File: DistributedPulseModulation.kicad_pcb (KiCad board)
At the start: 2 copper layers, 95.9 x 90.2 mm, 63 parts, among them IC1 SN7447a, J1 Conn_02x12_Odd_Even, J2 Conn_01x01, U1 74LS251, U10 4053, U11 4053, U12 4053, U2 4013, U25 74LS85, U28 74LS85, U31 74LS85, U4 MCP23017_SP, U7 4053, U8 4040, U9 4040

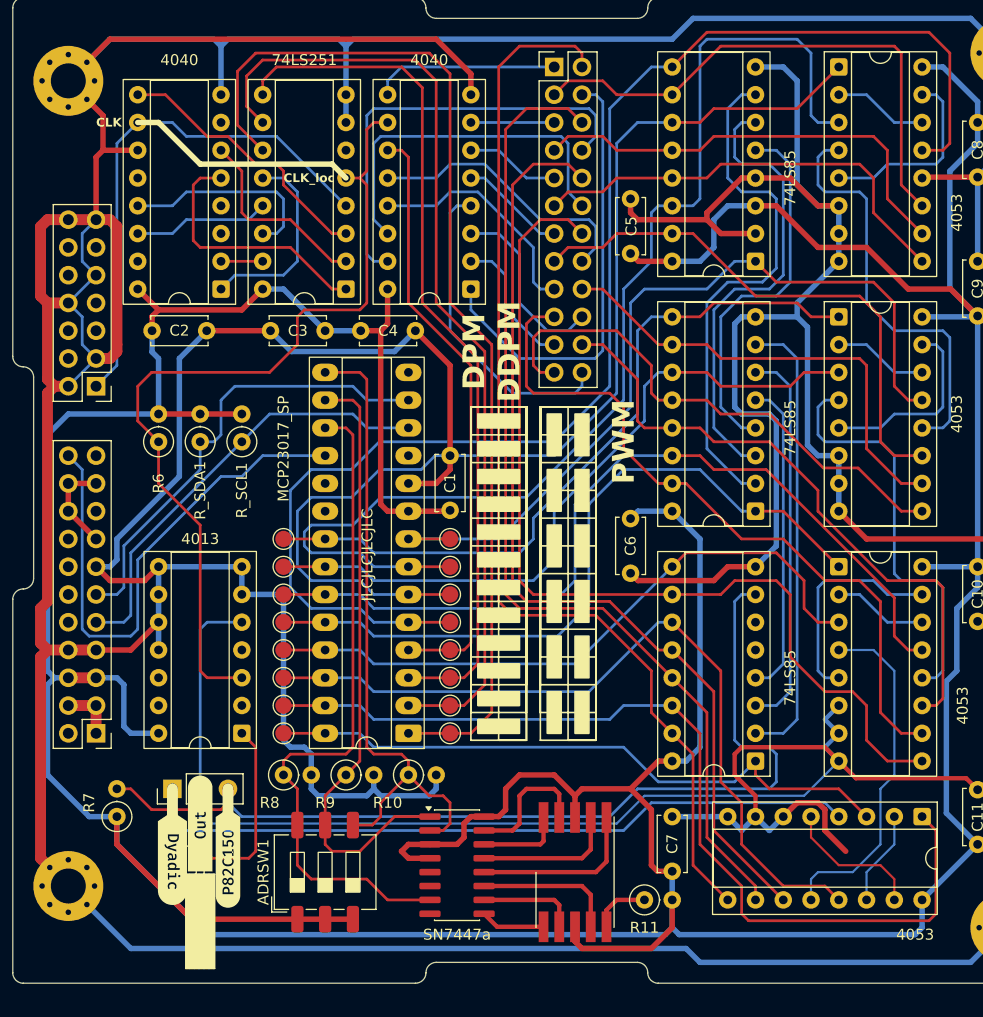
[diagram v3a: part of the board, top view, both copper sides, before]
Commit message: [update] : choix aficheurs et conv ; bug pin A1 ; condo ; doc pdf
- choix du 7-segment en common anode
- choix de decodeur DCBN vers 7-segments
- bug routage pin A1 sur V2.0 de la carte
- condo découplage sur D-latch
- condo découplage sur DVBN->7-segments
- ajout doc pdf work-in-progress
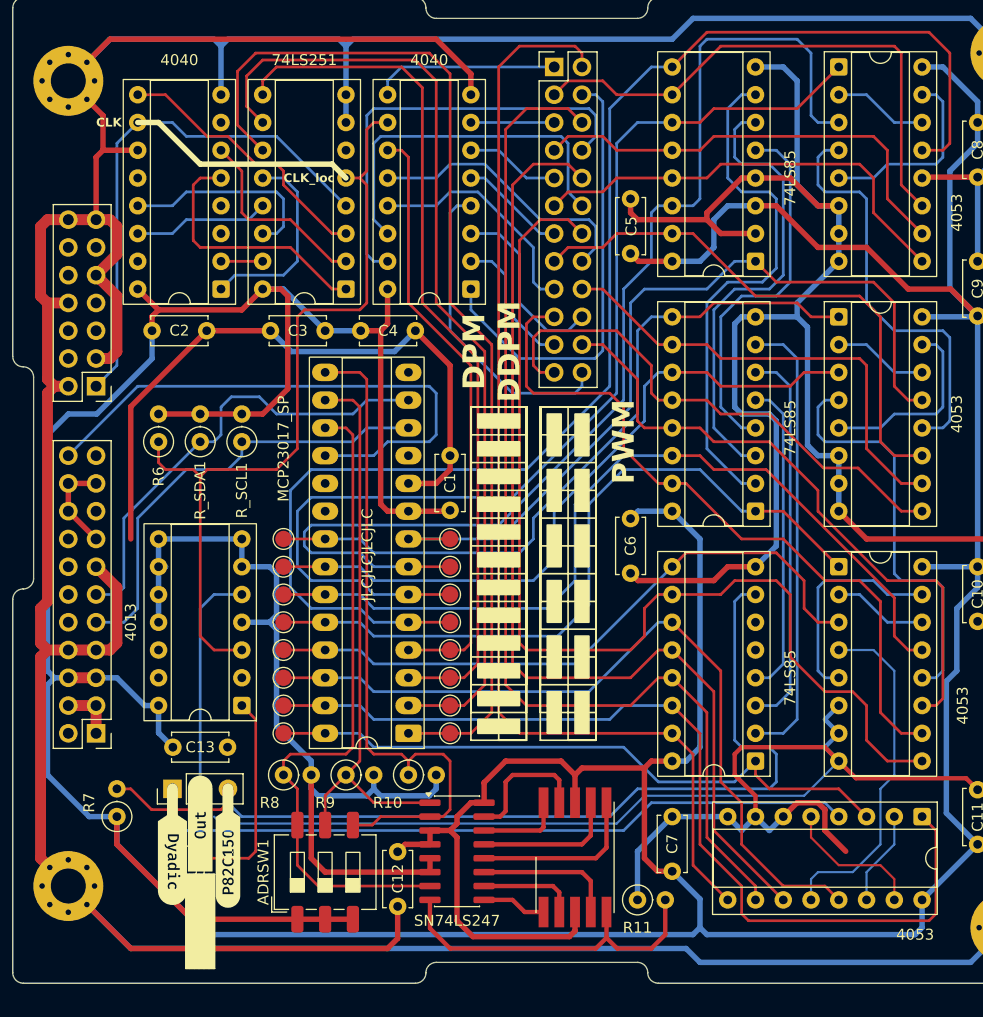
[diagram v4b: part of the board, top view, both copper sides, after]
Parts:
- added C12: 0.1µF, Capacitor_THT:C_Disc_D5.0mm_W2.5mm_P5.00mm, F.Cu at (76.5, 127.6)
- added C13: 0.1µF, Capacitor_THT:C_Disc_D5.0mm_W2.5mm_P5.00mm, F.Cu at (60.9, 113.0)
- DS1: value GS2011CR-G -> GS2011AR-G
- IC1: value SN7447a -> SN74LS247
- R11: value 2.2K -> 330
- moved U2 2.53 mm to (62.2, 109.2)
- moved DS1 1.35 mm to (92.7, 123.1)
- moved IC1 1.27 mm to (81.9, 122.6)
- moved R11 0.64 mm to (98.4, 127.0)
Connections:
- IC1 pad 8: Ground -> Net-(DS1-DP)
- R11 pad 1: Net-(DS1-DP) -> Ground
- R11 pad 2: +5V -> Net-(DS1-DP)
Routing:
- net Ground: track 866.4 -> 909.2 mm
- net Net-(DS1-DP): track 5.39 -> 31.8 mm
- net +5V: track 475.3 -> 497.1 mm
- net /CNT_A3: track 88.1 -> 97.1 mm
- net /CNT_A1: track 92.7 -> 99.7 mm
- net /CNT_A2: track 88.5 -> 94.7 mm
- net /ADR1: track 55.9 -> 51.7 mm
- net /Clock_loc: track 77.9 -> 73.9 mm
- net /CNT_A0: track 99.3 -> 103.0 mm
- net DPM: track 16.7 -> 19.2 mm
- net Net-(JP5-C): track 18.7 -> 20.8 mm
- net ~{Reset}: track 49.4 -> 51.3 mm
- net /ADR2: track 59.9 -> 61.6 mm
- net SCL: track 41.0 -> 42.2 mm
- net /ADR0: track 61.1 -> 60.6 mm
